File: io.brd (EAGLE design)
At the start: 23 x 40 mm, 34 parts, among them J1 SJ-3523-SMT-TR, Q1 MMBT2222A, Q2 2SCR574D3TL1TRANS_2SCR573_TO-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, U1 MCP1703T-5002E, U3 LM386M-1

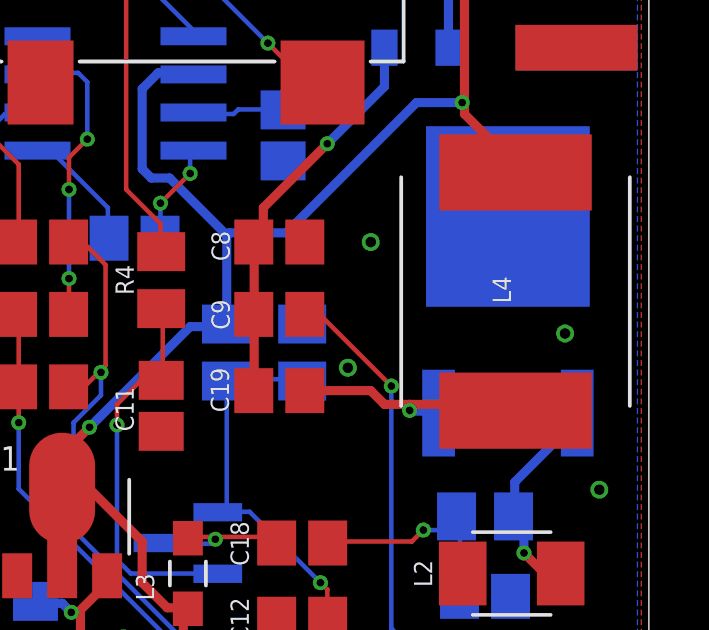
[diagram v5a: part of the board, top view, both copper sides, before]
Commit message: v1.1a of I/O board
* Q2 pinout was wrong, pins 2 and 3 were swapped
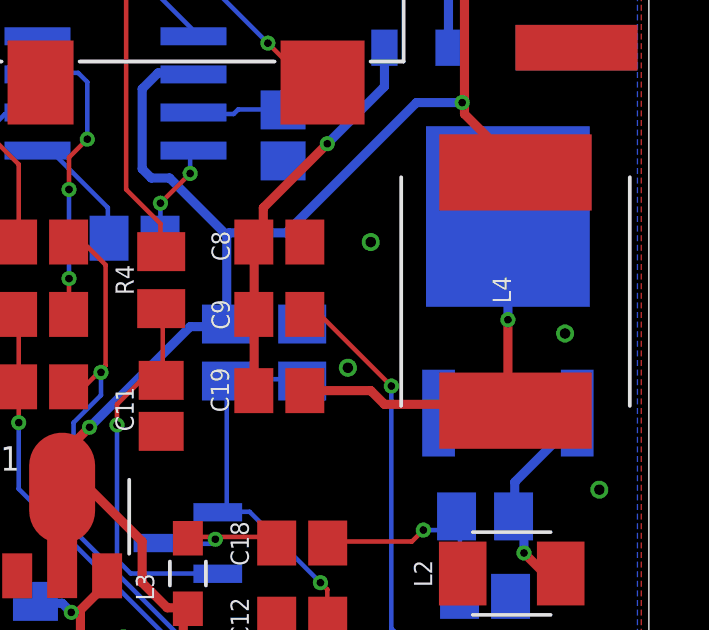
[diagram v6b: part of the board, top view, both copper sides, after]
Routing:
- net N$24: track 8.52 -> 13.9 mm
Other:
- board text added: "9VuTX IO Board v1.1a K6GG"
- board text removed: "9VuTX IO Board v1.1 K6GG"
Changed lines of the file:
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@@
 <layers>
 <layer number="1" name="Top" color="4" fill="1" visible="yes" active="yes"/>
-<layer number="16" name="Bottom" color="1" fill="1" visible="yes" active="yes"/>
+<layer number="16" name="Bottom" color="1" fill="1" visible="no" active="yes"/>
 <layer number="17" name="Pads" color="2" fill="1" visible="yes" active="yes"/>
 <layer number="18" name="Vias" color="2" fill="1" visible="yes" active="yes"/>
@@
 <layer number="20" name="Dimension" color="24" fill="1" visible="yes" active="yes"/>
 <layer number="21" name="tPlace" color="7" fill="1" visible="yes" active="yes"/>
-<layer number="22" name="bPlace" color="7" fill="1" visible="yes" active="yes"/>
+<layer number="22" name="bPlace" color="7" fill="1" visible="no" active="yes"/>
 <layer number="23" name="tOrigins" color="15" fill="1" visible="yes" active="yes"/>
-<layer number="24" name="bOrigins" color="15" fill="1" visible="yes" active="yes"/>
+<layer number="24" name="bOrigins" color="15" fill="1" visible="no" active="yes"/>
 <layer number="25" name="tNames" color="7" fill="1" visible="yes" active="yes"/>
-<layer number="26" name="bNames" color="7" fill="1" visible="yes" active="yes"/>
+<layer number="26" name="bNames" color="7" fill="1" visible="no" active="yes"/>
 <layer number="27" name="tValues" color="7" fill="1" visible="no" active="yes"/>
 <layer number="28" name="bValues" color="7" fill="1" visible="no" active="yes"/>
@@
 <layer number="38" name="bTest" color="7" fill="1" visible="no" active="yes"/>
 <layer number="39" name="tKeepout" color="4" fill="11" visible="yes" active="yes"/>
-<layer number="40" name="bKeepout" color="1" fill="11" visible="yes" active="yes"/>
+<layer number="40" name="bKeepout" color="1" fill="11" visible="no" active="yes"/>
 <layer number="41" name="tRestrict" color="4" fill="10" visible="yes" active="yes"/>
-<layer number="42" name="bRestrict" color="1" fill="10" visible="yes" active="yes"/>
+<layer number="42" name="bRestrict" color="1" fill="10" visible="no" active="yes"/>
 <layer number="43" name="vRestrict" color="2" fill="10" visible="no" active="yes"/>
 <layer number="44" name="Drills" color="7" fill="1" visible="no" active="yes"/>
@@
 <layer number="50" name="dxf" color="7" fill="1" visible="no" active="no"/>
 <layer number="51" name="tDocu" color="7" fill="1" visible="yes" active="yes"/>
-<layer number="52" name="bDocu" color="7" fill="1" visible="yes" active="yes"/>
+<layer number="52" name="bDocu" color="7" fill="1" visible="no" active="yes"/>
 <layer number="53" name="tGND_GNDA" color="7" fill="9" visible="no" active="no"/>
 <layer number="54" name="bGND_GNDA" color="1" fill="9" visible="no" active="no"/>
@@
 <wire x1="0" y1="40.005" x2="0" y2="0" width="0" layer="20"/>
 <text x="20.32" y="35.56" size="0.8128" layer="26" rot="MR0">9VuTX
-IO Board v1.1
+IO Board v1.1a
 K6GG</text>
 </plain>
@@
 <wire x1="13.716" y1="15.24" x2="11.518" y2="15.24" width="0.3048" layer="1"/>
 <wire x1="14.1732" y1="14.7828" x2="13.716" y2="15.24" width="0.3048" layer="1"/>
-<wire x1="18.3642" y1="14.7828" x2="15.0114" y2="14.7828" width="0.3048" layer="1"/>
-<wire x1="15.0114" y1="14.7828" x2="14.1732" y2="14.7828" width="0.3048" layer="1"/>
+<wire x1="18.3642" y1="14.7828" x2="14.1732" y2="14.7828" width="0.3048" layer="1"/>
 <wire x1="18.5166" y1="14.6304" x2="18.3642" y2="14.7828" width="0.3048" layer="1"/>
 <wire x1="18.5166" y1="14.6304" x2="18.542" y2="14.57198125" width="0.3048" layer="1"/>
-<wire x1="15.0368" y1="14.5542" x2="15.9258" y2="14.5542" width="0.3048" layer="16"/>
-<wire x1="15.0114" y1="14.5796" x2="15.0368" y2="14.5542" width="0.3048" layer="16"/>
-<wire x1="15.9258" y1="14.5542" x2="15.9766" y2="14.4907" width="0.3048" layer="16"/>
-<wire x1="15.0114" y1="14.5796" x2="15.0114" y2="14.7828" width="0.3048" layer="1"/>
-<via x="15.0114" y="14.5796" extent="1-16" drill="0.254"/>
+<wire x1="18.288" y1="17.6022" x2="18.288" y2="21.0439" width="0.3048" layer="16"/>
+<wire x1="18.288" y1="14.859" x2="18.288" y2="17.6022" width="0.3048" layer="1"/>
+<wire x1="18.288" y1="14.859" x2="18.542" y2="14.57198125" width="0.3048" layer="1"/>
+<via x="18.288" y="17.6022" extent="1-16" drill="0.254"/>
 </signal>
 <signal name="N$25" class="1">

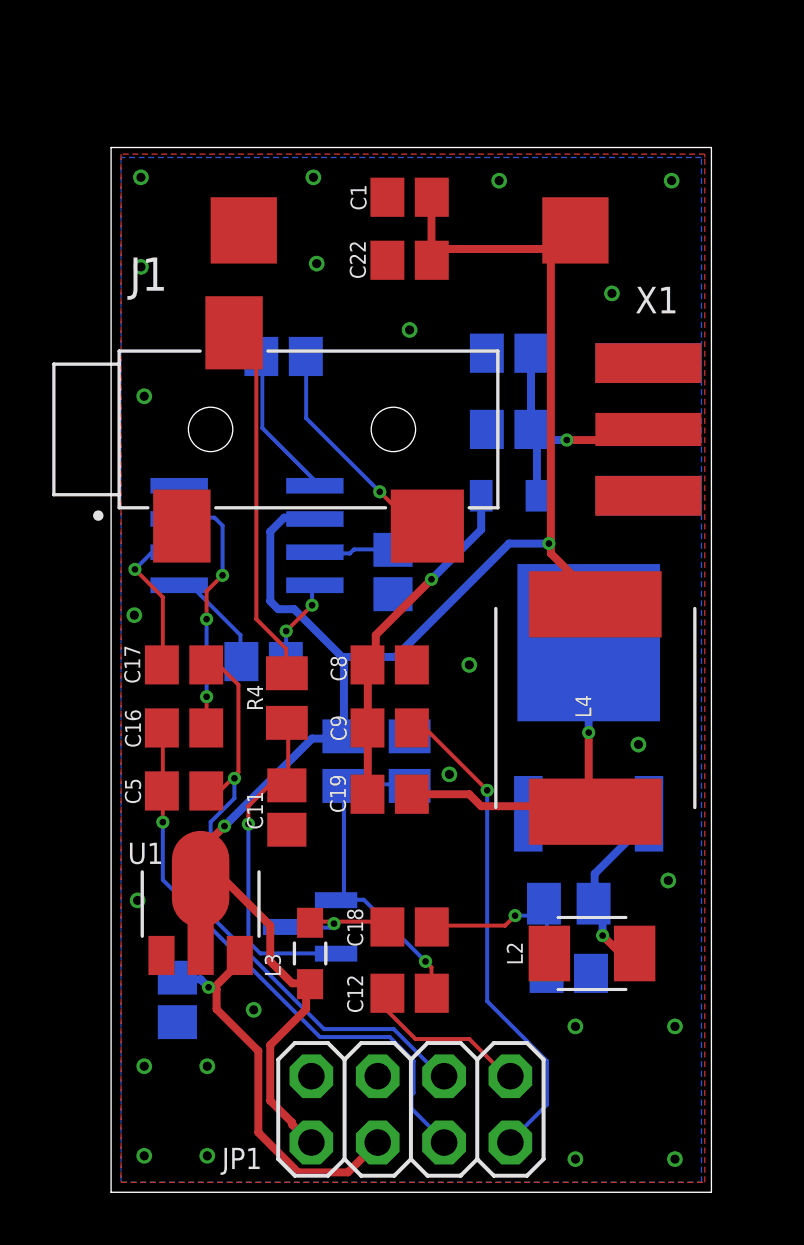
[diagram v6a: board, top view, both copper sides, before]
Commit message: Working on 1.1a of I/O after testing
* replaced L4 with a much smaller component
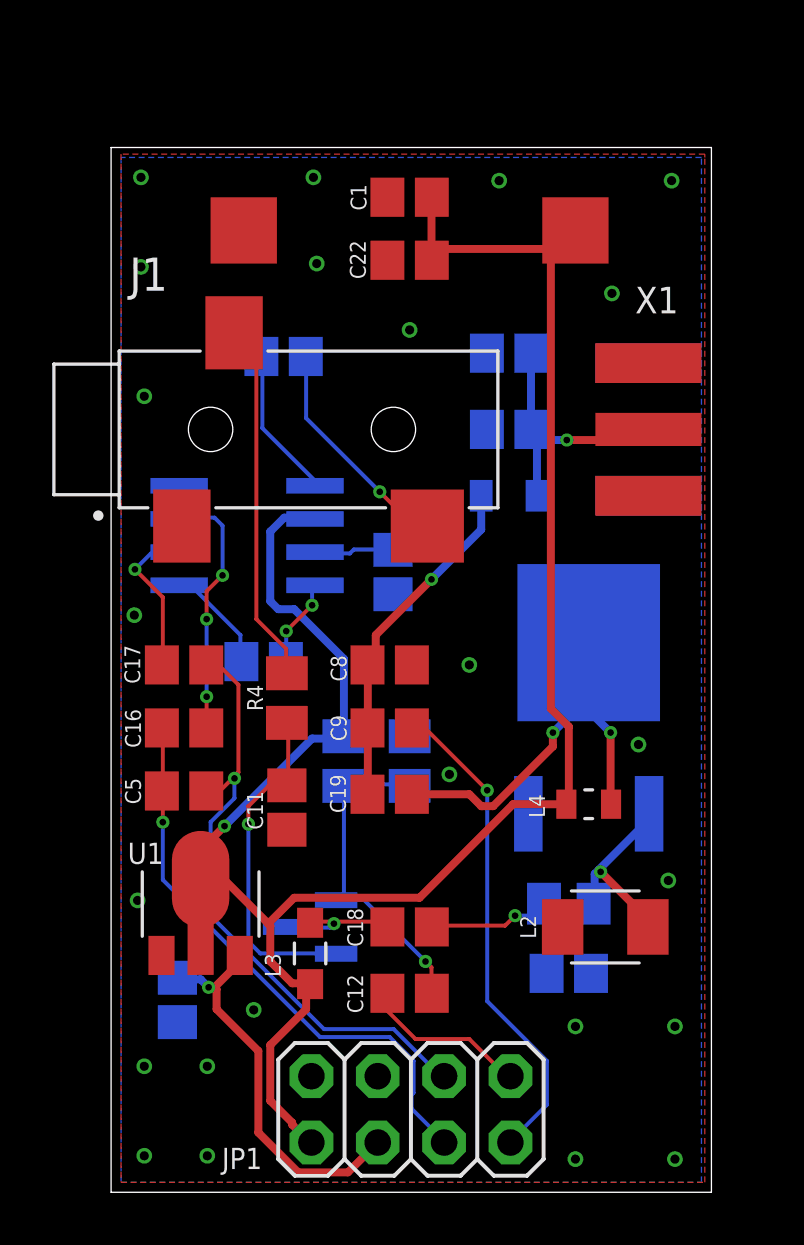
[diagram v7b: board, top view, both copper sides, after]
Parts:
- L4: device zort2:DS106C2 -> LQW18AN16NG8ZD:INDC1609X100N
- moved L4 3.69 mm to (18.3, 14.9), turned to 180 degrees
- moved L2 1.14 mm to (18.9, 10.2)
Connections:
- net N$24: now also L4.1; no longer L4.P$1
- net VIN: now also L4.2; no longer L4.P$2
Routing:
- net VIN: track 67.8 -> 79.9 mm, vias 2 -> 1
- net N$24: track 13.9 -> 17.9 mm, vias 1 -> 2
- net N$23: track 7.24 -> 8.55 mm

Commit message: Continuing on V1.1a of the I/O board
* re-placed Q1 on the layout
* updated images
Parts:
- Q1: value MMBT2222A -> MMBT2222A-7-FSOT-23_DIO-M
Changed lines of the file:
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@@
 <attribute name="VALUE" x="18.669" y="14.605" size="0.3048" layer="27" rot="R180"/>
-</element>
-<element name="Q1" library="zort2" package="SOT-23_DIO-M" value="MMBT2222A" x="7.62" y="10.16" smashed="yes" rot="MR270">
-<attribute name="BUILT_BY" value="EMA_UL_Team" x="7.62" y="10.16" size="1.778" layer="28" rot="MR270" display="off"/>
-<attribute name="MANUFACTURER_PART_NUMBER" value="MMBT2222A-7-F" x="7.62" y="10.16" size="1.778" layer="28" rot="MR270" display="off"/>
-<attribute name="NAME" x="6.35" y="12.0396" size="0.6096" layer="26" ratio="6" rot="SMR270"/>
-<attribute name="SOURCELIBRARY" value="DIODESINC_2_2015-08-18" x="7.62" y="10.16" size="1.778" layer="28" rot="MR270" display="off"/>
-<attribute name="VENDOR" value="Diodes Inc" x="7.62" y="10.16" size="1.778" layer="28" rot="MR270" display="off"/>
 </element>
 <element name="U$1" library="zort2" package="9V_968_PAD" value="9V_9689V_968_SMD" x="11.43" y="36.83" smashed="yes" rot="R270"/>
@@
 <attribute name="NAME" x="20.066" y="33.655" size="1.016" layer="25" ratio="18"/>
 <attribute name="VALUE" x="17.526" y="33.02" size="0.8128" layer="27" ratio="10"/>
+</element>
+<element name="Q1" library="zort2" package="SOT-23_DIO-M" value="MMBT2222A-7-FSOT-23_DIO-M" x="7.62" y="10.16" smashed="yes" rot="MR270">
+<attribute name="BUILT_BY" value="EMA_UL_Team" x="7.62" y="10.16" size="1.778" layer="28" rot="MR270" display="off"/>
+<attribute name="MANUFACTURER_PART_NUMBER" value="MMBT2222A-7-F" x="7.62" y="10.16" size="1.778" layer="28" rot="MR270" display="off"/>
+<attribute name="NAME" x="6.35" y="12.4206" size="0.8128" layer="26" ratio="6" rot="SMR270"/>
+<attribute name="SOURCELIBRARY" value="DIODESINC_2_2015-08-18" x="7.62" y="10.16" size="1.778" layer="28" rot="MR270" display="off"/>
+<attribute name="VENDOR" value="Diodes Inc" x="7.62" y="10.16" size="1.778" layer="28" rot="MR270" display="off"/>
 </element>
 </elements>
@@
 <contactref element="R5" pad="2"/>
 <contactref element="R6" pad="1"/>
-<contactref element="Q1" pad="1"/>
 <wire x1="11.43" y1="15.621" x2="8.9154" y2="15.621" width="0.1524" layer="16"/>
 <wire x1="8.9154" y1="15.621" x2="8.89" y2="15.56" width="0.1524" layer="16"/>
@@
 <wire x1="8.9154" y1="11.2014" x2="9.6774" y2="11.2014" width="0.1524" layer="16"/>
 <wire x1="12.2682" y1="7.62" x2="12.28" y2="7.62" width="0.1524" layer="1"/>
-<wire x1="8.6868" y1="11.2014" x2="8.6158" y2="11.185" width="0.1524" layer="16"/>
 <wire x1="8.9154" y1="11.2014" x2="8.9154" y2="15.5448" width="0.1524" layer="16"/>
 <wire x1="8.9154" y1="15.5448" x2="8.89" y2="15.56" width="0.1524" layer="16"/>
-<wire x1="8.9154" y1="11.2014" x2="8.6158" y2="11.185" width="0.1524" layer="16"/>
 <via x="12.0396" y="8.8392" extent="1-16" drill="0.254"/>
+<contactref element="Q1" pad="1"/>
+<wire x1="8.6868" y1="11.2014" x2="8.6158" y2="11.185" width="0.1524" layer="16"/>
 </signal>
 <signal name="N$20">
 <contactref element="C11" pad="1"/>
 <contactref element="R4" pad="2"/>
-<contactref element="Q1" pad="2"/>
 <wire x1="6.7818" y1="17.907" x2="6.7818" y2="15.621" width="0.1524" layer="1"/>
 <wire x1="6.7818" y1="15.621" x2="6.731" y2="15.582" width="0.1524" layer="1"/>
@@
 <wire x1="6.0198" y1="15.5448" x2="5.2578" y2="14.7828" width="0.1524" layer="1"/>
 <wire x1="6.7056" y1="15.5448" x2="6.0198" y2="15.5448" width="0.1524" layer="1"/>
-<wire x1="8.6106" y1="9.144" x2="8.6158" y2="9.135" width="0.1524" layer="16"/>
 <wire x1="6.7056" y1="15.5448" x2="6.731" y2="15.582" width="0.1524" layer="1"/>
 <via x="5.2578" y="14.097" extent="1-16" drill="0.254"/>
+<contactref element="Q1" pad="2"/>
+<wire x1="8.6106" y1="9.144" x2="8.6158" y2="9.135" width="0.1524" layer="16"/>
 </signal>
 <signal name="N$21">
 <contactref element="L3" pad="1"/>
 <contactref element="C18" pad="1"/>
-<contactref element="Q1" pad="3"/>
 <wire x1="10.3632" y1="10.3632" x2="8.5344" y2="10.3632" width="0.1524" layer="1"/>
 <wire x1="8.5344" y1="10.3632" x2="7.62" y2="10.3632" width="0.1524" layer="1"/>
@@
 <wire x1="8.5344" y1="10.287" x2="8.382" y2="10.1346" width="0.1524" layer="16"/>
 <wire x1="8.5344" y1="10.3632" x2="8.5344" y2="10.287" width="0.1524" layer="1"/>
+<via x="8.5344" y="10.287" extent="1-16" drill="0.254"/>
+<contactref element="Q1" pad="3"/>
 <wire x1="6.6294" y1="10.1346" x2="6.6242" y2="10.16" width="0.1524" layer="16"/>
-<via x="8.5344" y="10.287" extent="1-16" drill="0.254"/>
 </signal>
 <signal name="N$22">
